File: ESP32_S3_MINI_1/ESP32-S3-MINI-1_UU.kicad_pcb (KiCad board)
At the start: 2 copper layers, 20.3 x 47 mm, 53 parts, among them IC1 TPS6282533DMQR, IC2 BQ25185DLHR, J1 JST_2mm_LiPo, J2 USB4120-03-C, J3 Qwiic_Vertical, J4 Castellated_1x01, J5 Castellated_1x17, J6 Castellated_1x19, U2 ESP32-S3-MINI-1, U3 MAX17048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

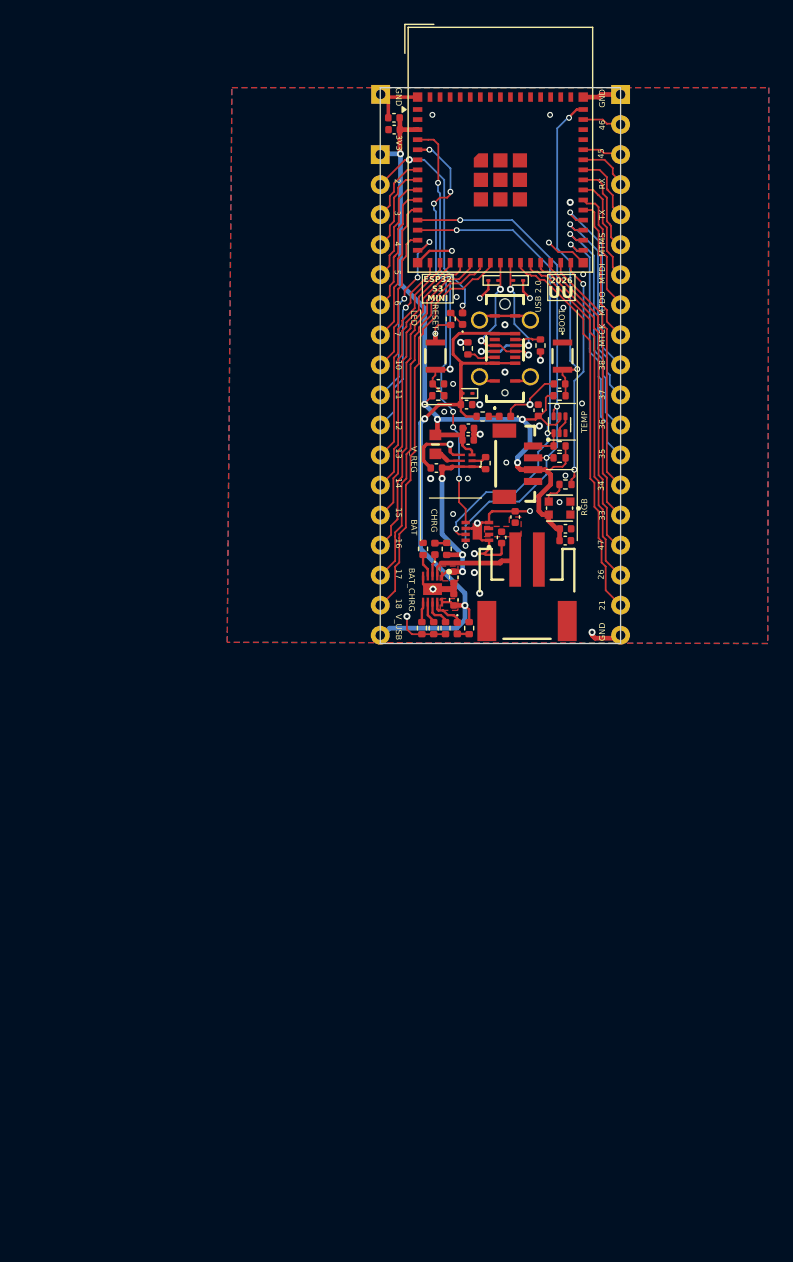
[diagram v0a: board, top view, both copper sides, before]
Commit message: ESP32-S3-1 updates from 1U design
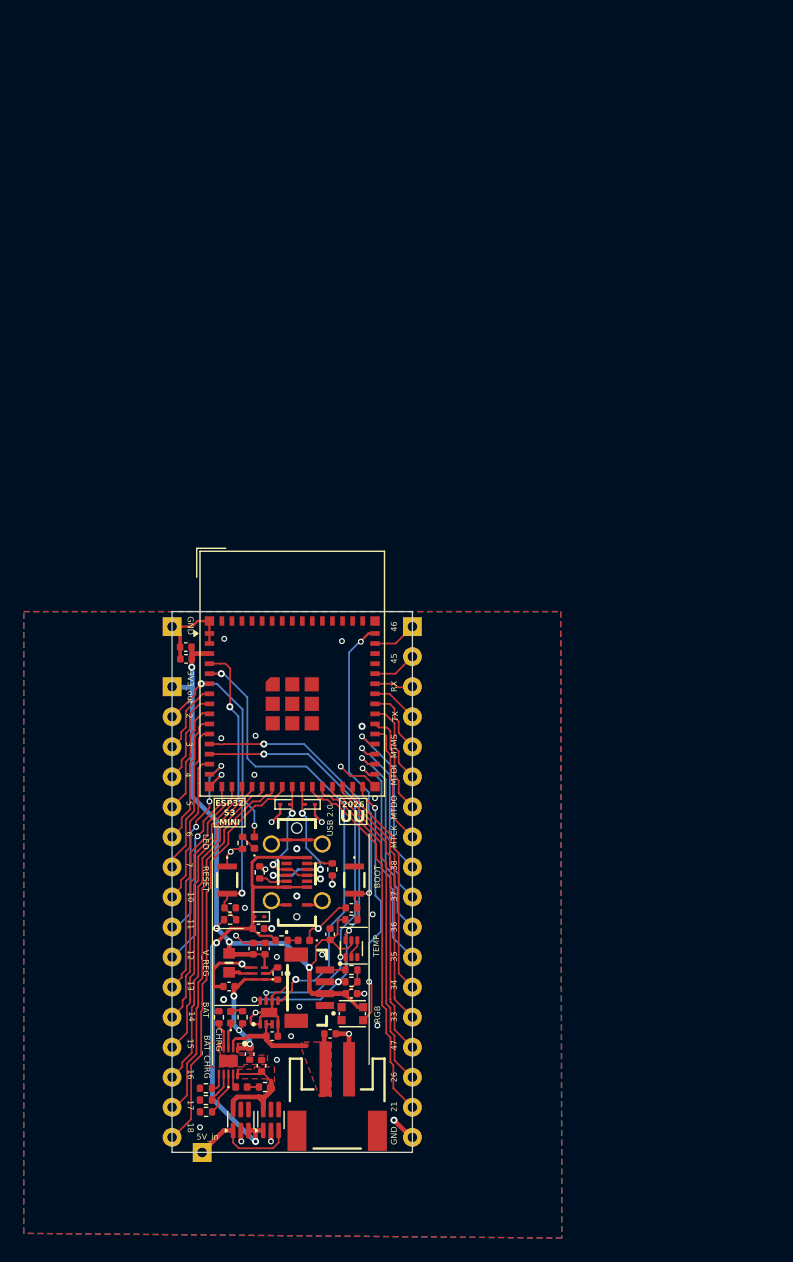
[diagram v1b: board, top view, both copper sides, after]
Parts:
- removed C13: 4.7uF, PCM_SparkFun-Capacitor:C_0402_1005Metric
- removed J5: Castellated_1x17, ESP32:Castellated_1x017_P2.54mm_D0.80mm
- removed J6: Castellated_1x19, ESP32:Castellated_1x019_P2.54mm_D0.80mm
- removed R15: 330, PCM_SparkFun-Resistor:R_0402_1005Metric
- added J7: Castellated_1x01, ESP32:Castellated_1x01_P2.54mm_D0.80mm, F.Cu at (174.8, 158.7)
- added J8: Castellated_1x16, Castellated_Connectors:Castellated_1x16_P2.54mm_D0.80mm, F.Cu at (172.2, 138.4)
- added J9: Castellated_1x18, Castellated_Connectors:Castellated_1x18_P2.54mm_D0.80mm, F.Cu at (192.6, 135.9)
- added U1: LM66100DCK, Package_TO_SOT_SMD:SOT-363_SC-70-6, F.Cu at (178.1, 156.0)
- added U5: LM66100DCK, Package_TO_SOT_SMD:SOT-363_SC-70-6, F.Cu at (180.6, 156.0)
- C4: value 0.1uF -> 0u1F
- moved J4 48.3 mm to (172.2, 114.3)
- moved C4 48.1 mm to (173.4, 117.0)
- moved C3 48.1 mm to (173.4, 116.0)
- moved C10 47.7 mm to (177.2, 138.1)
- moved C12 47.7 mm to (187.4, 138.1)
- moved D5 47.7 mm to (179.2, 132.5)
- moved D7 47.7 mm to (183.9, 129.3)
- moved D8 47.7 mm to (181.8, 129.3)
- moved J2 47.7 mm to (182.8, 135.1)
- moved J3 47.7 mm to (183.7, 144.8)
- moved R12 47.7 mm to (178.2, 132.6)
- moved R13 47.7 mm to (177.2, 139.1)
- moved R14 47.7 mm to (187.4, 143.3)
- moved R16 47.7 mm to (187.4, 144.3)
- moved R17 47.7 mm to (187.4, 139.1)
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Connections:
- net VSYS renamed V_SYS
- C8 pad 1: V_USB -> 5V
- D6 pad 3: Net-(D6-DIN) -> RGB
- IC2 pad 10: V_USB -> 5V
- R10 pad 2: V_USB -> 5V
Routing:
- net 5V: track 0.00 -> 12.2 mm
- net V_USB: track 52.1 -> 42.3 mm
- net 5V_IN: track 0.00 -> 9.59 mm
- net GND: track 71.2 -> 63.1 mm
- net 3V3: track 69.8 -> 61.7 mm, vias 5 -> 4
- net V_SYS: track 16.6 -> 11.4 mm
- net SCL: track 43.7 -> 39.5 mm
- net VBAT: track 9.19 -> 12.9 mm
- net SDA: track 44.9 -> 41.4 mm
- net BAT_ALRT: track 35.8 -> 39.2 mm, vias 6 -> 2
- net Net-(D6-DIN): track 2.12 -> 0.00 mm
- net IO47: track 27.0 -> 25.1 mm
- net TX: track 5.89 -> 3.96 mm
- net IO36: track 19.4 -> 17.5 mm
- net IO38: track 16.3 -> 14.4 mm
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- added copper zone on F.Cu, net 5V
- removed copper zone on F.Cu, net V_USB
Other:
- board size 20.3 x 47 mm -> 20.3 x 45.7 mm
- board text added: "3V3_out"
- board text added: "5V_in"
- board text removed: "3V3"
- board text removed: "V_USB"

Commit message: BOM update
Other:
- board text removed: "CHRG"
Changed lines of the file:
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@@
 		)
 		(embedded_fonts no)
-		(model "${ESP32}/NANOT160AS.step"
+		(model "${LOCAL}/NANOT160AS.step"
 			(offset
 				(xyz -1.049999937 -0.8199999805 0)
@@
 		)
 		(embedded_fonts no)
-		(model "${ESP32}/NANOT160AS.step"
+		(model "${LOCAL}/NANOT160AS.step"
 			(offset
 				(xyz -1.049999937 -0.8199999805 0)
@@
 		)
 		(embedded_fonts no)
-		(model "${ESP32}/TPS6282533DMQR.step"
+		(model "${LOCAL}/TPS6282533DMQR.step"
 			(offset
 				(xyz 0 0 0)
@@
 			)
 			(justify left bottom)
-		)
-	)
-	(gr_text "CHRG"
-		(at 175.9 148.2 270)
-		(layer "F.SilkS")
-		(effects
-			(font
-				(size 0.5 0.5)
-				(thickness 0.1)
-			)
-			(justify left bottom)
